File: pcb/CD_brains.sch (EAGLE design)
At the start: 21 parts, among them SW2 ROTARTY_ENCODER, U1 TC4422AVOA, U2 LCD-16X2SILK

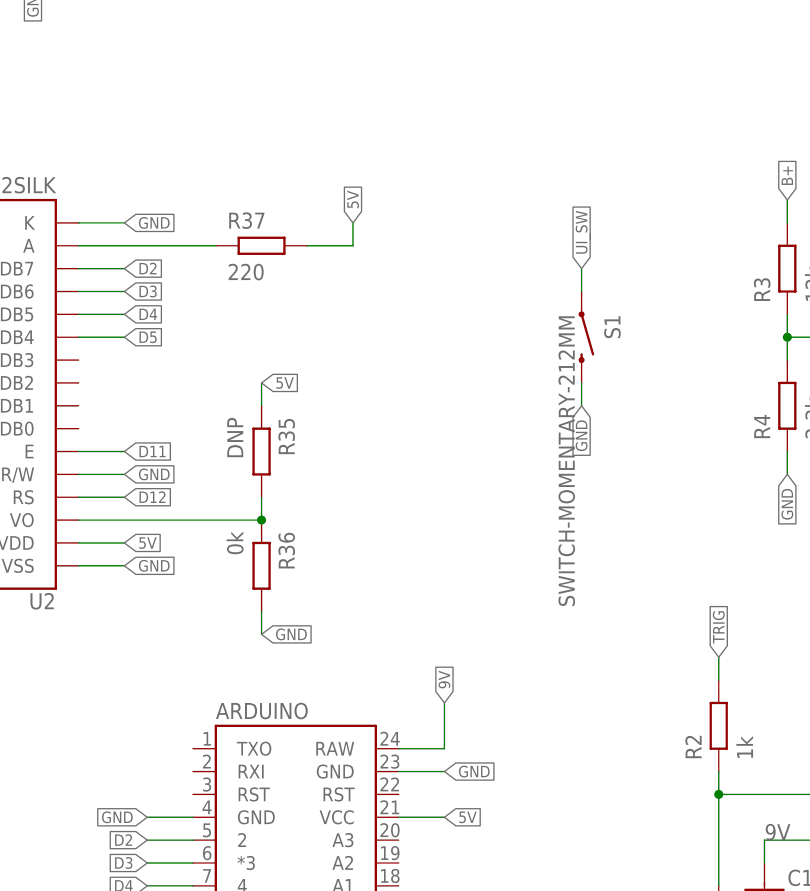
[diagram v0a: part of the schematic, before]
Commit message: fixed CD BRAINS Inconsistencies
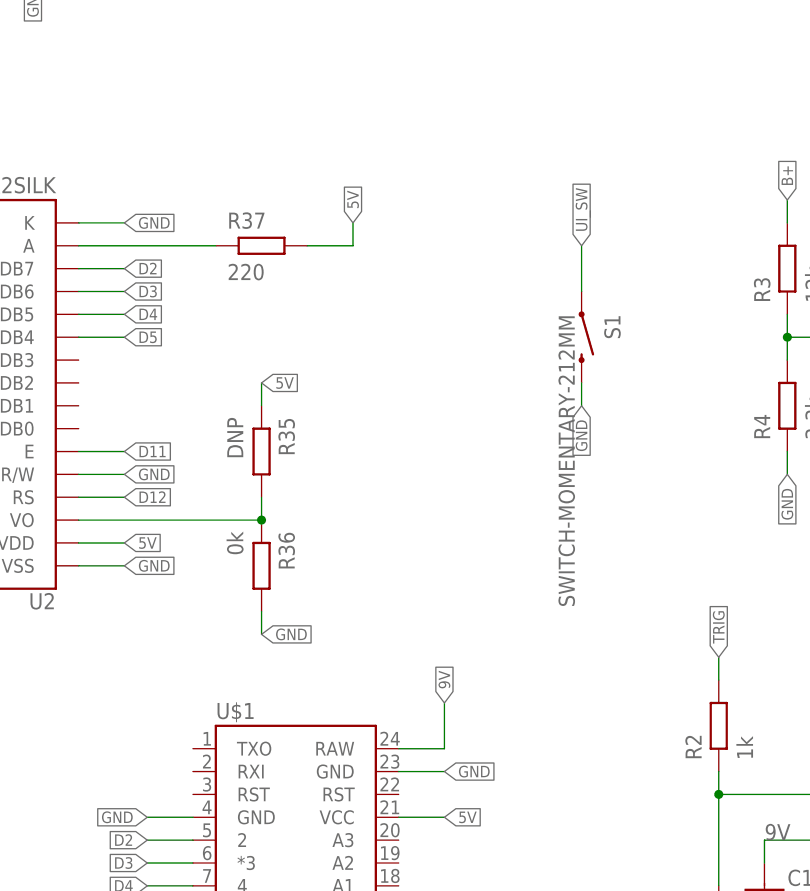
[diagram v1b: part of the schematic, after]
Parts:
- renumbered ARDUINO to U$1
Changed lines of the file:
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@@
 </classes>
 <parts>
-<part name="ARDUINO" library="_my-parts" deviceset="ARDUINO_PRO_MINI" device=""/>
 <part name="FRAME1" library="SparkFun-Aesthetics" deviceset="FRAME-A4L" device=""/>
 <part name="U1" library="Microchip_By_element14_Batch_1" deviceset="TC4422AVOA" device=""/>
@@
 <part name="R4" library="passives-7351" deviceset="RESISTOR" device="0603-N" value="3.3k"/>
 <part name="J3" library="SparkFun-Connectors" deviceset="M02" device="LOCK"/>
+<part name="U$1" library="_my-parts" deviceset="ARDUINO_PRO_MINI" device=""/>
 </parts>
 <sheets>
@@
 </plain>
 <instances>
-<instance part="ARDUINO" gate="G$1" x="50.8" y="38.1"/>
 <instance part="FRAME1" gate="G$1" x="0" y="0"/>
 <instance part="U1" gate="A" x="147.32" y="45.72"/>
@@
 <instance part="R4" gate="G$1" x="106.68" y="91.44" rot="R90"/>
 <instance part="J3" gate="G$1" x="58.42" y="139.7"/>
+<instance part="U$1" gate="G$1" x="50.8" y="38.1"/>
 </instances>
 <busses>
 </busses>
 <nets>
-<net name="UI_SW" class="0">
-<segment>
-<pinref part="S1" gate="G$1" pin="1"/>
-<wire x1="83.82" y1="104.14" x2="83.82" y2="106.68" width="0.1524" layer="91"/>
-<label x="83.82" y="106.68" size="1.27" layer="95" rot="R90" xref="yes"/>
-</segment>
-<segment>
-<pinref part="ARDUINO" gate="G$1" pin="*10"/>
-<wire x1="63.5" y1="25.4" x2="68.58" y2="25.4" width="0.1524" layer="91"/>
-<label x="68.58" y="25.4" size="1.27" layer="95" xref="yes"/>
-</segment>
-</net>
 <net name="FT_SW" class="0">
 <segment>
-<pinref part="ARDUINO" gate="G$1" pin="8"/>
 <wire x1="40.64" y1="27.94" x2="35.56" y2="27.94" width="0.1524" layer="91"/>
 <label x="35.56" y="27.94" size="1.27" layer="95" rot="R180" xref="yes"/>
+<pinref part="U$1" gate="G$1" pin="8"/>
 </segment>
 <segment>
@@
 <net name="9V" class="0">
 <segment>
-<pinref part="ARDUINO" gate="G$1" pin="RAW"/>
 <wire x1="63.5" y1="53.34" x2="68.58" y2="53.34" width="0.1524" layer="91"/>
 <wire x1="68.58" y1="53.34" x2="68.58" y2="58.42" width="0.1524" layer="91"/>
 <label x="68.58" y="58.42" size="1.27" layer="95" rot="R90" xref="yes"/>
+<pinref part="U$1" gate="G$1" pin="RAW"/>
 </segment>
 <segment>
@@
 <net name="GND" class="0">
 <segment>
-<pinref part="ARDUINO" gate="G$1" pin="GND@2"/>
 <wire x1="63.5" y1="50.8" x2="68.58" y2="50.8" width="0.1524" layer="91"/>
 <label x="68.58" y="50.8" size="1.27" layer="95" xref="yes"/>
+<pinref part="U$1" gate="G$1" pin="GND@2"/>
 </segment>
 <segment>
@@
 </segment>
 <segment>
-<pinref part="ARDUINO" gate="G$1" pin="GND"/>
 <wire x1="40.64" y1="45.72" x2="35.56" y2="45.72" width="0.1524" layer="91"/>
 <label x="35.56" y="45.72" size="1.27" layer="95" rot="R180" xref="yes"/>
+<pinref part="U$1" gate="G$1" pin="GND"/>
 </segment>
 <segment>
@@
 <net name="5V" class="0">
 <segment>
-<pinref part="ARDUINO" gate="G$1" pin="VCC"/>
 <wire x1="63.5" y1="45.72" x2="68.58" y2="45.72" width="0.1524" layer="91"/>
 <label x="68.58" y="45.72" size="1.27" layer="95" xref="yes"/>
+<pinref part="U$1" gate="G$1" pin="VCC"/>
 </segment>
 <segment>
@@
 <net name="ENC_01" class="0">
 <segment>
-<pinref part="ARDUINO" gate="G$1" pin="*6"/>
 <wire x1="40.64" y1="33.02" x2="35.56" y2="33.02" width="0.1524" layer="91"/>
 <label x="35.56" y="33.02" size="1.27" layer="95" rot="R180" xref="yes"/>
+<pinref part="U$1" gate="G$1" pin="*6"/>
 </segment>
 <segment>
@@
 <net name="ENC_02" class="0">
 <segment>
-<pinref part="ARDUINO" gate="G$1" pin="7"/>
 <wire x1="40.64" y1="30.48" x2="35.56" y2="30.48" width="0.1524" layer="91"/>
 <label x="35.56" y="30.48" size="1.27" layer="95" rot="R180" xref="yes"/>
+<pinref part="U$1" gate="G$1" pin="7"/>
 </segment>
 <segment>
@@
 </segment>
 <segment>
-<pinref part="ARDUINO" gate="G$1" pin="2"/>
 <wire x1="40.64" y1="43.18" x2="35.56" y2="43.18" width="0.1524" layer="91"/>
 <label x="35.56" y="43.18" size="1.27" layer="95" rot="R180" xref="yes"/>
+<pinref part="U$1" gate="G$1" pin="2"/>
 </segment>
 </net>
@@
 </segment>
 <segment>
-<pinref part="ARDUINO" gate="G$1" pin="*3"/>
 <wire x1="40.64" y1="40.64" x2="35.56" y2="40.64" width="0.1524" layer="91"/>
 <label x="35.56" y="40.64" size="1.27" layer="95" rot="R180" xref="yes"/>
+<pinref part="U$1" gate="G$1" pin="*3"/>
 </segment>
 </net>
@@
 </segment>
 <segment>
-<pinref part="ARDUINO" gate="G$1" pin="4"/>
 <wire x1="40.64" y1="38.1" x2="35.56" y2="38.1" width="0.1524" layer="91"/>
 <label x="35.56" y="38.1" size="1.27" layer="95" rot="R180" xref="yes"/>
+<pinref part="U$1" gate="G$1" pin="4"/>
 </segment>
 </net>
@@
 </segment>
 <segment>
-<pinref part="ARDUINO" gate="G$1" pin="*5"/>
 <wire x1="40.64" y1="35.56" x2="35.56" y2="35.56" width="0.1524" layer="91"/>
 <label x="35.56" y="35.56" size="1.27" layer="95" rot="R180" xref="yes"/>
+<pinref part="U$1" gate="G$1" pin="*5"/>
 </segment>
 </net>
@@
 <net name="CAP_V_IN" class="0">
 <segment>
-<pinref part="ARDUINO" gate="G$1" pin="A0"/>
 <wire x1="63.5" y1="35.56" x2="68.58" y2="35.56" width="0.1524" layer="91"/>
 <label x="68.58" y="35.56" size="1.27" layer="95" xref="yes"/>
+<pinref part="U$1" gate="G$1" pin="A0"/>
 </segment>
 <segment>
@@
 </segment>
 <segment>
-<pinref part="ARDUINO" gate="G$1" pin="*9"/>
 <wire x1="40.64" y1="25.4" x2="35.56" y2="25.4" width="0.1524" layer="91"/>
 <label x="35.56" y="25.4" size="1.27" layer="95" rot="R180" xref="yes"/>
+<pinref part="U$1" gate="G$1" pin="*9"/>
 </segment>
 </net>
 <net name="D12" class="0">
 <segment>
-<pinref part="ARDUINO" gate="G$1" pin="12"/>
 <wire x1="63.5" y1="30.48" x2="68.58" y2="30.48" width="0.1524" layer="91"/>
 <label x="68.58" y="30.48" size="1.27" layer="95" xref="yes"/>
+<pinref part="U$1" gate="G$1" pin="12"/>
 </segment>
 <segment>
@@
 <net name="D11" class="0">
 <segment>
-<pinref part="ARDUINO" gate="G$1" pin="*11"/>
 <wire x1="63.5" y1="27.94" x2="68.58" y2="27.94" width="0.1524" layer="91"/>
 <label x="68.58" y="27.94" size="1.27" layer="95" xref="yes"/>
+<pinref part="U$1" gate="G$1" pin="*11"/>
 </segment>
 <segment>
@@
 </segment>
 </net>
+<net name="UI_SW" class="0">
+<segment>
+<wire x1="63.5" y1="25.4" x2="68.58" y2="25.4" width="0.1524" layer="91"/>
+<pinref part="U$1" gate="G$1" pin="*10"/>
+<label x="68.58" y="25.4" size="1.27" layer="95" xref="yes"/>
+</segment>
+<segment>
+<pinref part="S1" gate="G$1" pin="1"/>
+<wire x1="83.82" y1="104.14" x2="83.82" y2="109.22" width="0.1524" layer="91"/>
+<label x="83.82" y="109.22" size="1.27" layer="95" rot="R90" xref="yes"/>
+</segment>
+</net>
